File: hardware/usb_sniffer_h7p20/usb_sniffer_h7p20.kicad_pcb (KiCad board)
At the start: 4 copper layers, 45 x 45 mm, 146 parts, among them J1 FPGA_JTAG, J2 USB_C_Receptacle_USB2.0_16P, J3 USB_A, J4 USB_C_Receptacle_USB2.0_16P, J5 FFC-40P-0.5mm,NC, U1 H7P20N0L128-M3H1, U11 EA3036C, U2 LM2903, U3 LM2903, U4 LM2903, U5 USB3343, U6 P25Q32SH-SSH-IT, U7 CY7C68013A-56LTX, U8 24C64BN, U9 CJ3439KDW, X1 XO32,26M,NC, Y1 26M,NC, Y2 24M

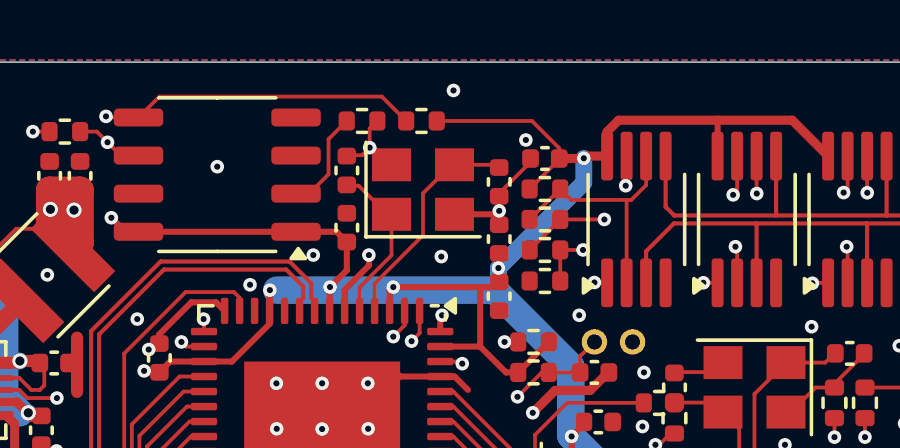
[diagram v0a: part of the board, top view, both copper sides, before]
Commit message: [usb_sniffer_h7p20] 68013的eeprom增加boot点，用于二次更新68013固件
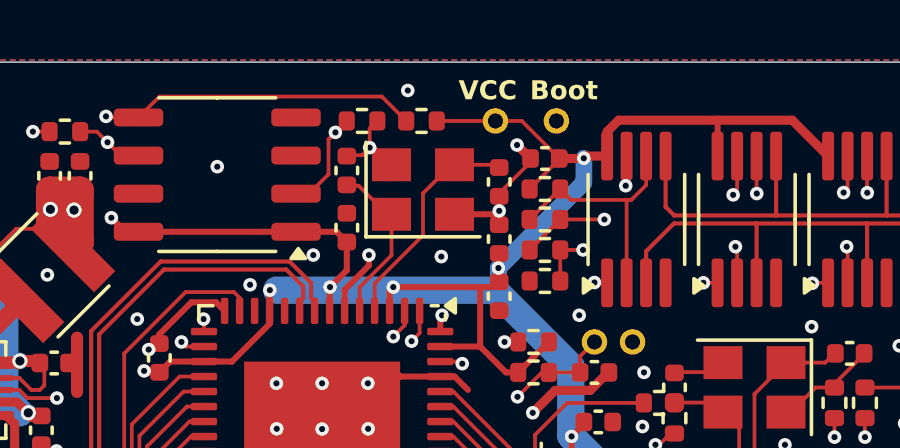
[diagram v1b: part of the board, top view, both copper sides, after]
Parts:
- added TP14: TestPoint, vllogic:PinHeader_1x01_P1.00mm_Vertical, F.Cu at (113.4, 77.0)
- added TP15: TestPoint, vllogic:PinHeader_1x01_P1.00mm_Vertical, F.Cu at (115.4, 77.0)
- moved G*** 0.66 mm to (107.6, 84.3)
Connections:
- net Net-(U8-A1) renamed /Boot
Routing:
- net /Boot: track 3.38 -> 11.5 mm, vias 0 -> 1
- net GND: track 87.4 -> 88.0 mm
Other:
- board text added: "Boot"
- board text added: "VCC"

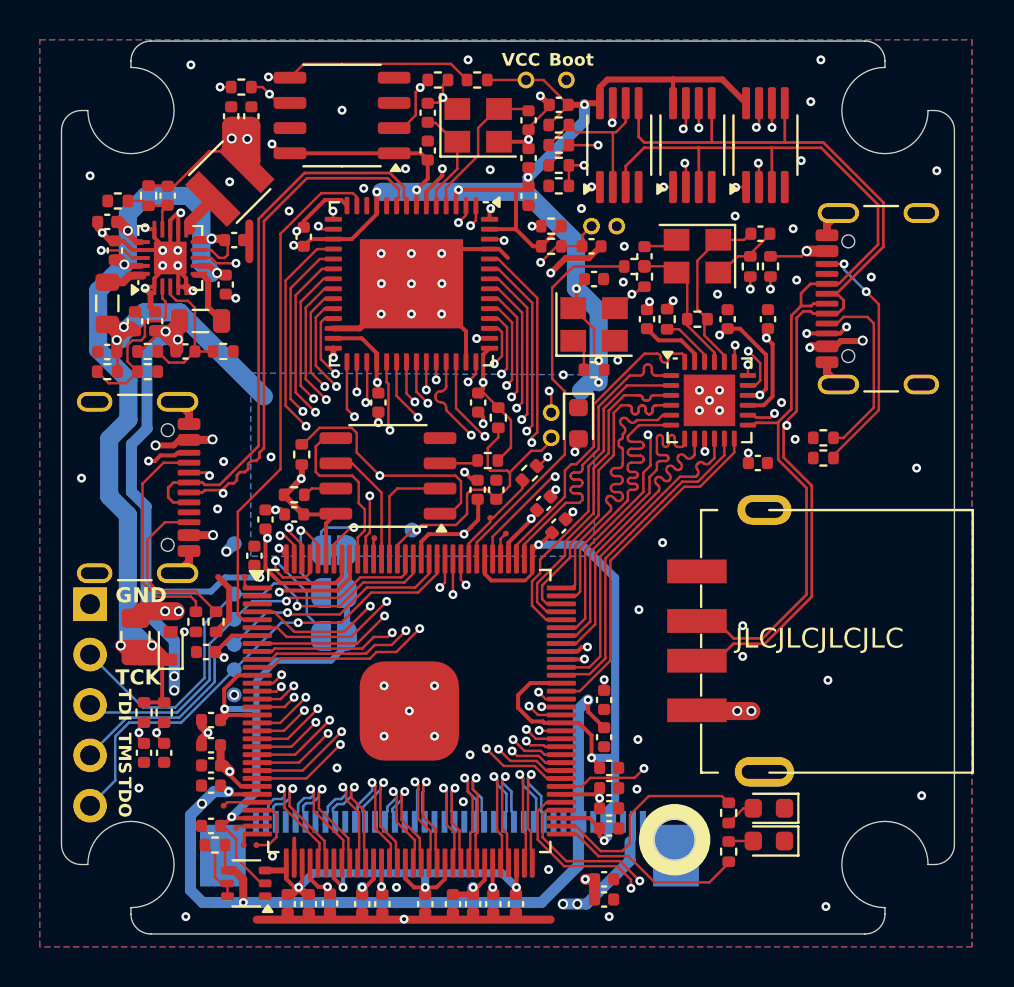
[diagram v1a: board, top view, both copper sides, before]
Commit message: [usb_sniffer_h7p20] 预留外部触发接口，优化布局，支持M4隔离柱
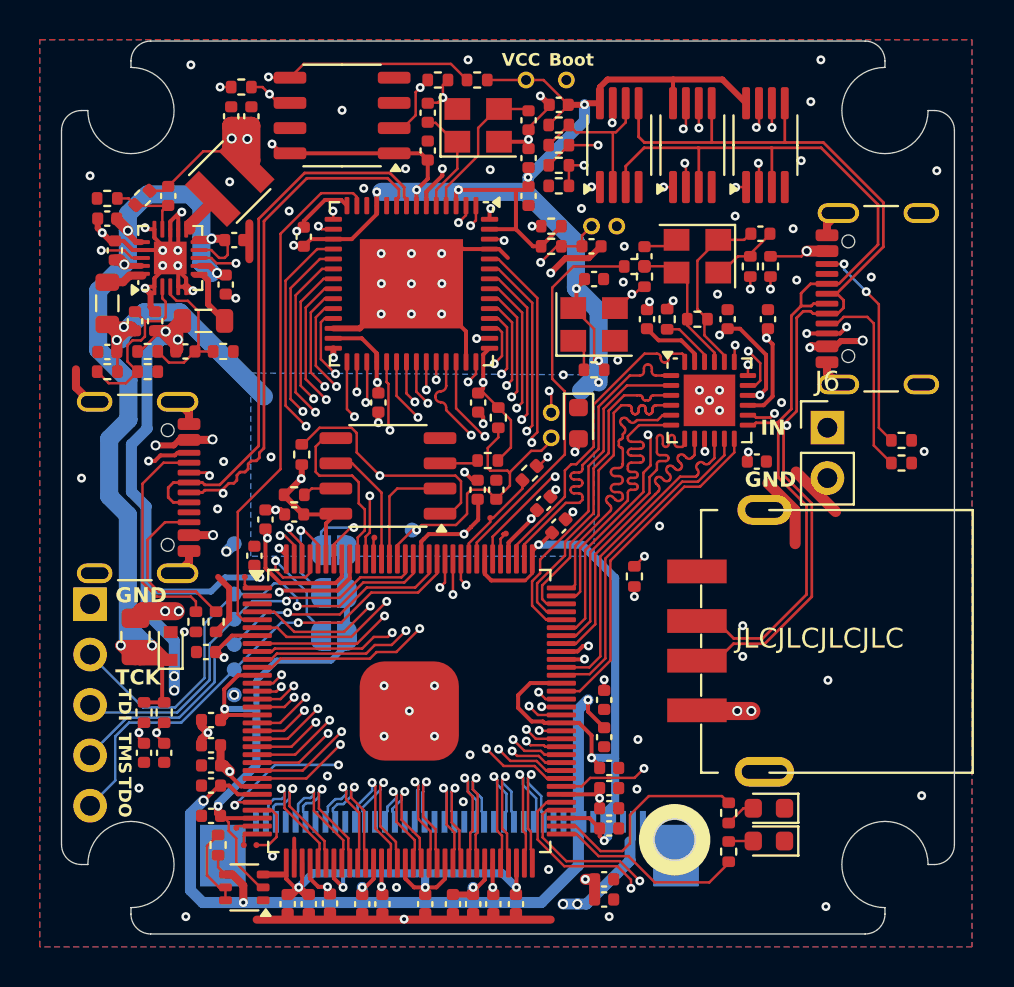
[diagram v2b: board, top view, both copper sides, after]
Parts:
- removed TP19, TP5: TestPoint, vllogic:TestPoint_Pad_D0.3mm
- added J6: Trigger, Connector_PinHeader_2.54mm:PinHeader_1x02_P2.54mm_Vertical, F.Cu at (128.6, 94.5)
- added R7: 470, Resistor_SMD:R_0402_1005Metric, F.Cu at (118.9, 102.0)
- added TP17: TestPoint, vllogic:TestPoint_Pad_D0.3mm, F.Cu at (105.8, 100.0)
- C1: value 0.1uF -> NC
- moved R26 4.14 mm to (132.3, 96.3), turned to 0 degrees
- moved R25 4.04 mm to (132.3, 95.1), turned to 0 degrees
- moved R39 0.55 mm to (92.3, 82.9)
- moved C42 0.51 mm to (97.5, 114.0)
- moved R40 0.33 mm to (94.1, 82.9), turned to 45 degrees
- moved U9 0.23 mm to (99.2, 117.7)
- moved C26 0.17 mm to (92.3, 83.9)
- moved R24 0.15 mm to (97.9, 115.5), turned to -90 degrees
- moved L3 0.15 mm to (97.2, 89.1)
- moved C8 0.09 mm to (125.0, 96.2)
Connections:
- U1 pad 28: Net-(U1-IO17_7) -> /TRIGGER
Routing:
- net /TRIGGER: track 0.00 -> 28.5 mm, vias 0 -> 3
- net Net-(J6-Pin_1): track 0.00 -> 12.6 mm, vias 0 -> 1
- net GND: track 88.0 -> 96.8 mm, vias 101 -> 99
- net /VDD_CORE: track 125.2 -> 127.3 mm
- net Net-(U1-IO17_7): track 1.77 -> 0.00 mm
- net Net-(J2-CC2): track 12.3 -> 10.7 mm
- net /VCC_3V3: track 213.6 -> 214.7 mm
- net /VCCAUX: track 101.0 -> 100.1 mm, vias 13 -> 12
- net Net-(U9-D1): track 3.24 -> 4.10 mm
- net Net-(U11-FB1): track 3.44 -> 3.94 mm
- net Net-(J2-CC1): track 9.54 -> 10.0 mm
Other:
- board text added: "IN"

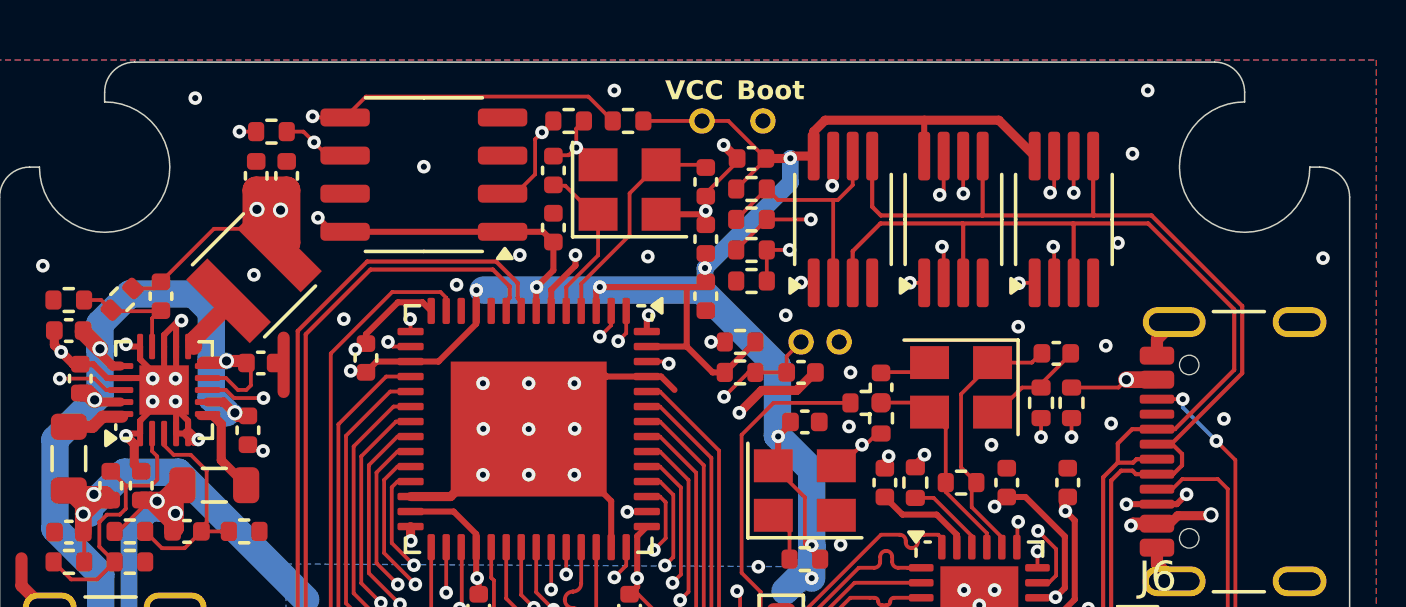
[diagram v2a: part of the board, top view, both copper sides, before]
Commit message: [usb_sniffer_h7p20] 使用USB5V驱动LM2903
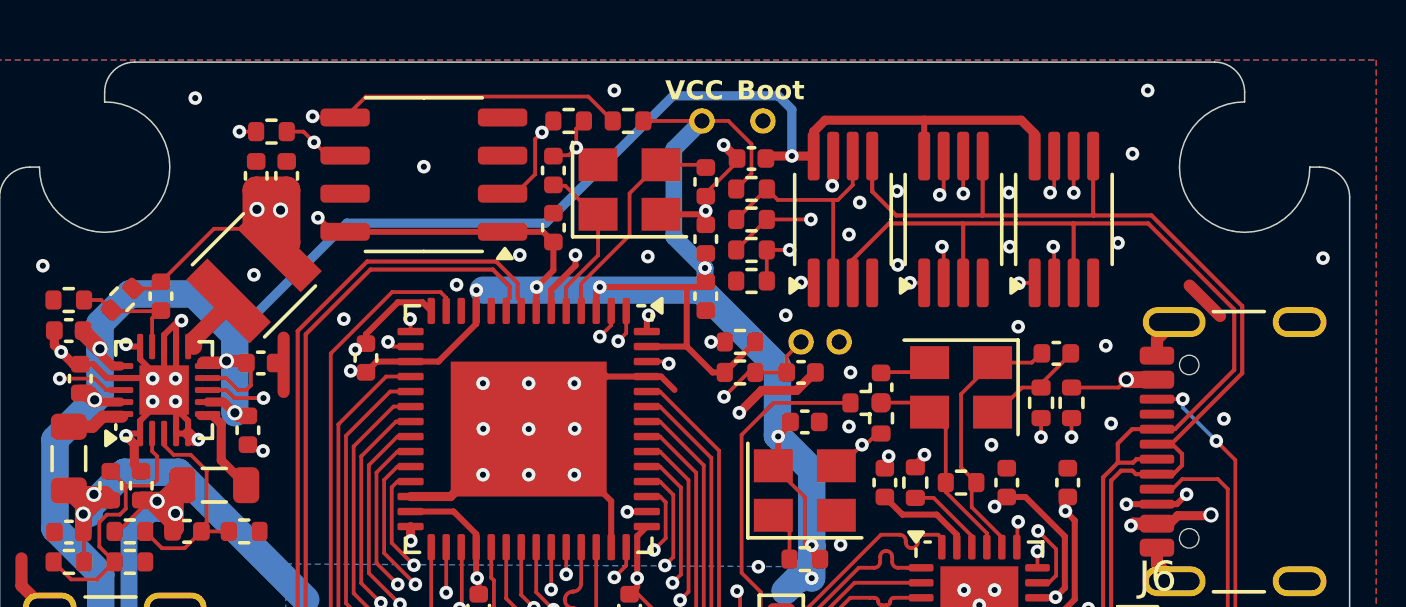
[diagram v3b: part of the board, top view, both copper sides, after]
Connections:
- net /TRIGGER renamed /IN
- C3 pad 2: /VCC_3V3 -> /VCC_5V
- U2 pad 8: /VCC_3V3 -> /VCC_5V
- U3 pad 8: /VCC_3V3 -> /VCC_5V
- U4 pad 8: /VCC_3V3 -> /VCC_5V
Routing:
- net /VCC_5V: track 100.2 -> 135.3 mm, vias 9 -> 10
- net /VCC_3V3: track 214.7 -> 203.5 mm, vias 28 -> 27
- net GND: track 96.8 -> 98.2 mm, vias 99 -> 105

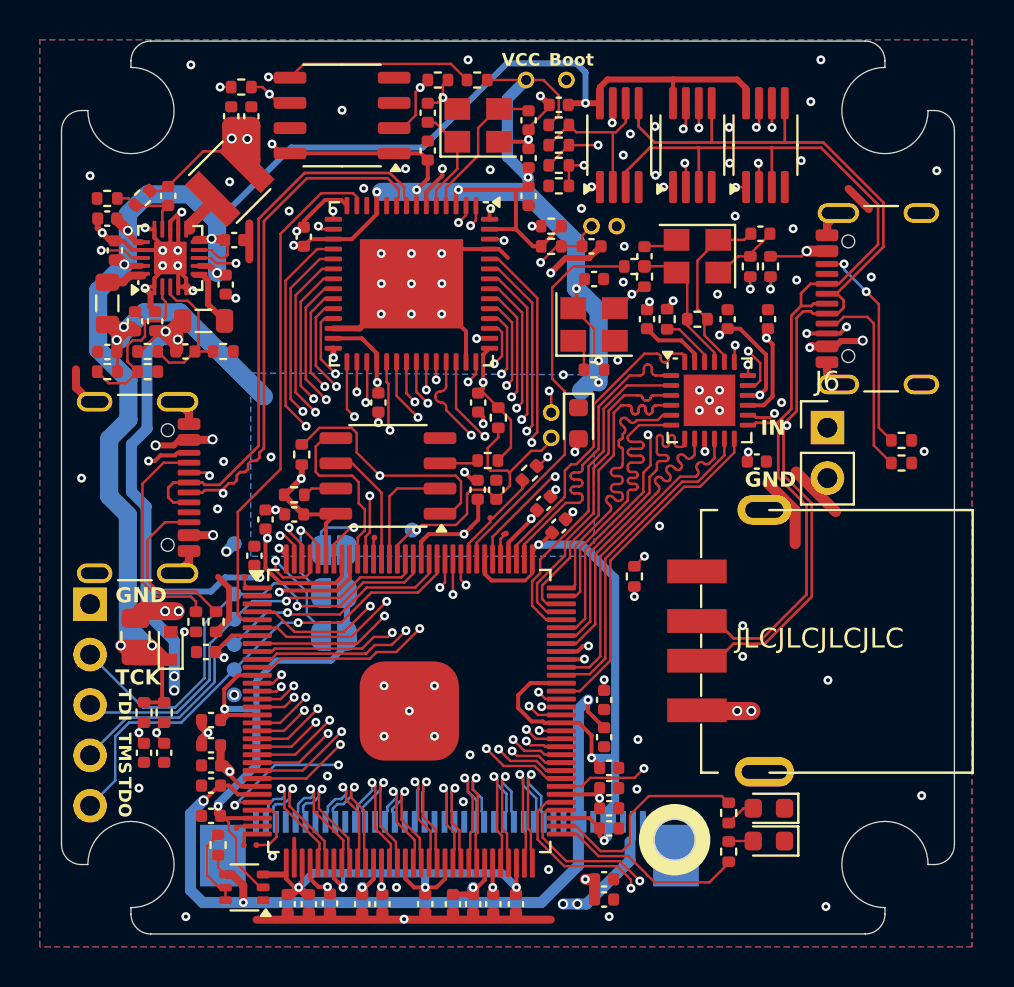
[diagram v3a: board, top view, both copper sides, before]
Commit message: [usb_sniffer_h7p20] 移除NC器件，更换LM2903A-VR，双螺丝孔固定
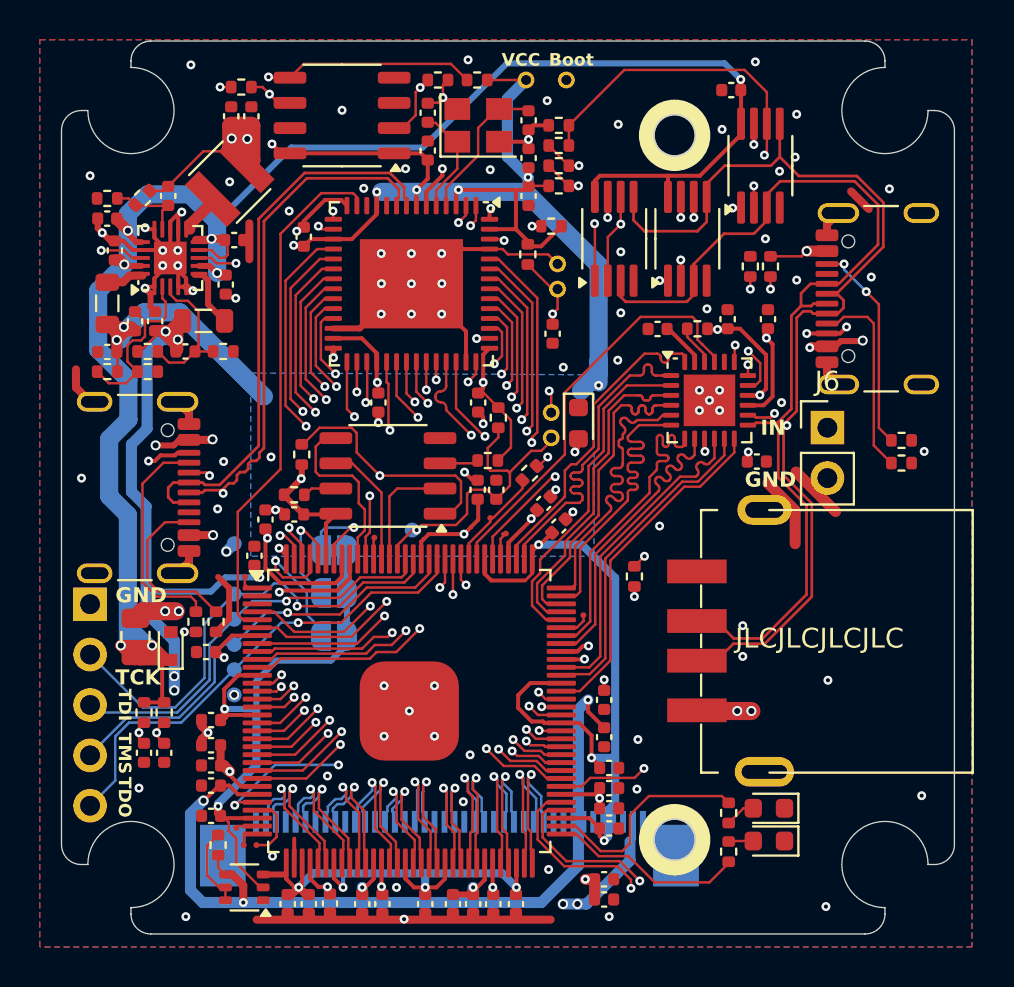
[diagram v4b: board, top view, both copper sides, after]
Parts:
- removed C1, C5, C7: NC, Capacitor_SMD:C_0402_1005Metric
- removed R1, R27, R29: NC, Resistor_SMD:R_0402_1005Metric
- removed R14: 33, Resistor_SMD:R_0402_1005Metric
- removed X1: XO32,26M,NC, vllogic:OSC_3225
- removed Y1: 26M,NC, vllogic:OSC_3225
- added TP5: TestPoint, vllogic:TestPoint_Pad_D0.3mm, F.Cu at (116.3, 103.9)
- U2, U3, U4: value LM2903 -> LM2903A-VR
- moved C3 8.72 mm to (123.8, 77.5)
- moved C35 4.82 mm to (114.8, 89.8), turned to 90 degrees
- moved U3 4.72 mm to (121.5, 85.0)
- moved U4 4.72 mm to (117.9, 85.0)
- moved TP4 3.60 mm to (115.0, 87.5), turned to 90 degrees
- moved TP3 3.54 mm to (115.0, 86.2), turned to 90 degrees
- moved R20 3.07 mm to (115.1, 82.3)
- moved R23 3.05 mm to (115.1, 79.2)
- moved R31 1.60 mm to (122.0, 89.5), turned to 180 degrees
- moved R4 1.25 mm to (113.5, 85.8), turned to -90 degrees
- moved U2 1.07 mm to (125.2, 81.3)
- moved R21 1.03 mm to (115.1, 81.3)
- moved R22 1.00 mm to (115.1, 80.3)
- moved C9 0.73 mm to (120.0, 89.5), turned to 0 degrees
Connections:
- U1 pad 91: /XO32_26M -> Net-(U1-IO12_PCLK_3)
- U5 pad 20: Net-(U5-XO) -> unconnected-(U5-XO-Pad20)
- U5 pad 21: /USB334x_26M -> /FPGA_OUT_26M
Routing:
- net /XO32_26M: track 21.6 -> 0.00 mm, vias 2 -> 0
- net /VCC_3V3: track 203.5 -> 192.2 mm, vias 27 -> 24
- net Net-(U5-XO): track 9.03 -> 0.00 mm
- net GND: track 98.2 -> 90.7 mm, vias 105 -> 98
- net /VCC_5V: track 135.3 -> 142.6 mm
- net /USB334x_26M: track 7.05 -> 0.00 mm
- net /USB20_DP_CMP2: track 23.3 -> 19.2 mm
- net /USB334x/CMP_REF_1: track 15.5 -> 18.7 mm, vias 3 -> 2
- net /USB20_DP_CMP3: track 26.2 -> 28.6 mm
- net /USB20_DM_CMP3: track 29.9 -> 27.9 mm
- net Net-(X1-EN): track 1.68 -> 0.00 mm
- net Net-(U1-IO12_PCLK_3): track 0.00 -> 1.54 mm
- net /USB20_DM_CMP2: track 65.4 -> 66.9 mm
- net Net-(U7-~{RESET}): track 12.6 -> 11.3 mm
- net /USB334x/CMP_REF_3: track 8.39 -> 9.58 mm, vias 0 -> 2
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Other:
- outline, holes or cut-outs redrawn

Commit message: [usb_sniffer_h7p20] 优化USB封装精度，优化定位孔精度
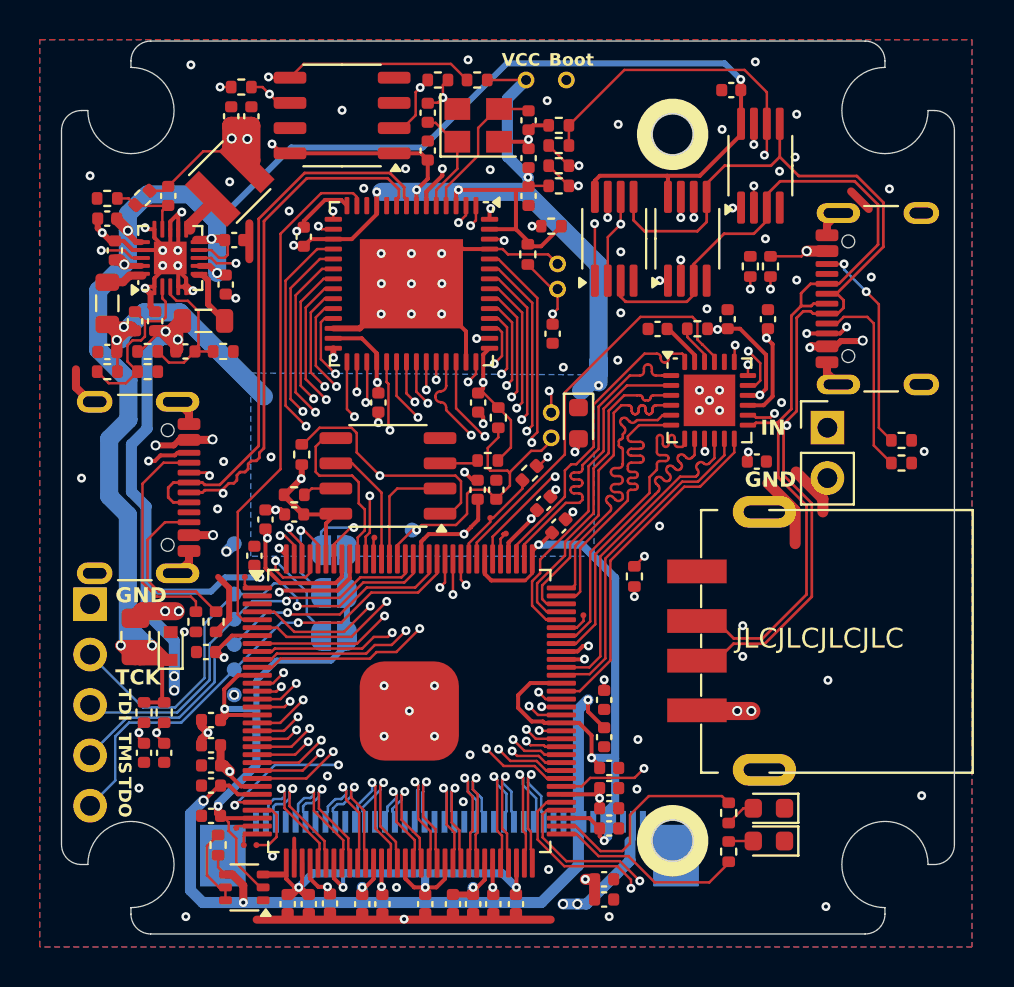
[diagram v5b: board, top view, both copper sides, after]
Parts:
- J2, J4: footprint Connector_USB:USB_C_Receptacle_GCT_USB4105-xx-A_16P_TopMnt_Horizontal -> vllogic:USB_C_Receptacle_16P
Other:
- outline, holes or cut-outs redrawn
